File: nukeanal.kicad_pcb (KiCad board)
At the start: 2 copper layers, 85 x 56 mm, 2 parts, among them P1 CONN_13X2

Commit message: finished with schematic, footprint assignment, but no board yet
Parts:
- removed P1: CONN_13X2, pin_array_13x2
- removed sot-89: Q***, 111kicad-jake:sot-89
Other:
- board outline removed
- board text removed: "1/8" JACK OK WITH STD HEADERS !NO TH ABOVE!"
- board text removed: "DOUBLE USB CUTOUT FOR ALL BOARDS"
- board text removed: "RASPBERRY-PI ADDON BOARD VIEW FROM TOP NOTE: P1 SHOULD BE FITTED ON THE REVERSE OF THE BOARD"
- board text removed: "RCA REMOVE WITH STD HEADERS !NO TH ABOVE!"
- board text removed: "RJ45 CUTOUT FOR STD HEADERS !NO TH ABOVE!"

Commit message: merge from .zip download of jerry's latest commit
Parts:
- added C1: 100, SMD_Packages:SM0805, F.Cu at (227.0, 187.2)
- added C10: 101, SMD_Packages:SM0805, F.Cu at (200.0, 110.0)
- added C11: 104, SMD_Packages:SM0805, F.Cu at (168.8, 130.0)
- added C12: 225, SMD_Packages:SM0805, F.Cu at (165.5, 145.2)
- added C13: 225, SMD_Packages:SM0805, F.Cu at (168.8, 118.8)
- added C14: 104, SMD_Packages:SM0805, F.Cu at (165.5, 149.8)
- added C15: 225, SMD_Packages:SM0805, F.Cu at (165.5, 147.5)
- added C16: 225, SMD_Packages:SM0805, F.Cu at (232.0, 185.8)
- added C17: 225, SMD_Packages:SM0805, F.Cu at (232.0, 183.5)
- added C18: 104, SMD_Packages:SM0805, F.Cu at (177.0, 112.8)
- added C19: 225, SMD_Packages:SM0805, F.Cu at (177.0, 115.0)
- added C2: 100, SMD_Packages:SM0805, F.Cu at (197.0, 115.5)
- added C20: 104, SMD_Packages:SM0805, F.Cu at (177.0, 121.8)
- added C21: 225, SMD_Packages:SM0805, F.Cu at (177.0, 124.0)
- added C22: 104, SMD_Packages:SM0805, F.Cu at (177.0, 126.2)
- added C23: 225, SMD_Packages:SM0805, F.Cu at (177.0, 128.5)
- added C24: 104, SMD_Packages:SM0805, F.Cu at (172.5, 130.0)
- added C25: 225, SMD_Packages:SM0805, F.Cu at (172.5, 132.2)
- added C26: 104, SMD_Packages:SM0805, F.Cu at (177.0, 117.2)
- added C27: 225, SMD_Packages:SM0805, F.Cu at (177.0, 119.5)
- added C28: 104, SMD_Packages:SM0805, F.Cu at (168.8, 121.0)
- added C29: 225, SMD_Packages:SM0805, F.Cu at (168.8, 132.2)
- added C3: 225, SMD_Packages:SM0805, F.Cu at (246.8, 166.8)
- added C30: 104, SMD_Packages:SM0805, F.Cu at (173.0, 125.5)
- added C31: 225, SMD_Packages:SM0805, F.Cu at (173.0, 123.2)
- added C32: 104, SMD_Packages:SM0805, F.Cu at (177.0, 110.5)
- added C33: 225, SMD_Packages:SM0805, F.Cu at (177.0, 108.2)
- added C4: 101, SMD_Packages:SM0805, F.Cu at (252.8, 144.0)
- added C5: 104, SMD_Packages:SM0805, F.Cu at (243.2, 174.8)
- added C6: 471 poly, Capacitors_ThroughHole:Capacitor13x4RM10, F.Cu at (181.2, 135.2)
- added C7: 391, SMD_Packages:SM0805, F.Cu at (173.2, 127.8)
- added C8: 226, Capacitors:CP_5x6mm, F.Cu at (237.0, 168.0)
- added C9: 221, SMD_Packages:SM0805, F.Cu at (170.8, 172.2)
- added CU1: 104, SMD_Packages:SM0805, F.Cu at (168.8, 116.5)
- added CU2: 225, SMD_Packages:SM0805, F.Cu at (168.8, 114.2)
- added CU3: 104, SMD_Packages:SM0805, F.Cu at (228.2, 183.5)
- added CU4: 225, SMD_Packages:SM0805, F.Cu at (173.2, 119.2)
- added CU41: 104, SMD_Packages:SM0805, F.Cu at (168.8, 127.8)
- added CU5: 104, SMD_Packages:SM0805, F.Cu at (168.8, 123.2)
- added CU6: 225, SMD_Packages:SM0805, F.Cu at (168.8, 125.5)
- added CU7: 104, SMD_Packages:SM0805, F.Cu at (228.2, 181.2)
- added D1: 1N5819, Diodes_ThroughHole:Diode_DO-41_SOD81_Horizontal_RM10, F.Cu at (233.2, 161.0)
- added D10: 1N4148, Diodes_ThroughHole:Diode_DO-35_SOD27_Horizontal_RM10, F.Cu at (245.8, 156.2)
- added D11: 1N4148, Diodes_ThroughHole:Diode_DO-35_SOD27_Horizontal_RM10, F.Cu at (223.0, 117.5)
- added D12: 1N4148, Diodes_ThroughHole:Diode_DO-35_SOD27_Horizontal_RM10, F.Cu at (183.5, 172.2)
- added D13: 1N4148, Diodes_ThroughHole:Diode_DO-35_SOD27_Horizontal_RM10, F.Cu at (223.0, 124.0)
- added D14: 1N4148, Diodes_ThroughHole:Diode_DO-35_SOD27_Horizontal_RM10, F.Cu at (186.0, 167.0)
- added D2: 1N5819, Diodes_ThroughHole:Diode_DO-41_SOD81_Horizontal_RM10, F.Cu at (225.0, 176.2)
- added D3: DPAD1, 111kicad-jerry:TO-78_Housing_5Pin, F.Cu at (234.5, 150.2)
- added D5: 6.2V, Diodes_ThroughHole:Diode_DO-35_SOD27_Horizontal_RM10, F.Cu at (173.5, 165.2)
- added D6: 1N4007, Diodes_ThroughHole:Diode_DO-41_SOD81_Horizontal_RM10, F.Cu at (173.5, 148.0)
- added D7: 1N4007, Diodes_ThroughHole:Diode_DO-41_SOD81_Horizontal_RM10, F.Cu at (196.0, 175.8)
- added D8: 1N4148, Diodes_ThroughHole:Diode_DO-35_SOD27_Horizontal_RM10, F.Cu at (183.5, 177.5)
- added D9: 1N4148, Diodes_ThroughHole:Diode_DO-35_SOD27_Horizontal_RM10, F.Cu at (245.8, 151.0)
- added K1: CONN_3, Connect:SIL-3, F.Cu at (153.2, 191.4)
- added P1: BNC, 111kicad-jerry:bnc-rocket, F.Cu at (141.4, 191.2)
- added P2: CONN_1, 111kicad-jerry:testpin037, F.Cu at (197.2, 187.0)
- added P3: CONN_6, 111kicad-jerry:6x1pin037, F.Cu at (185.2, 153.5)
- added P4: CONN_2, Connect:bornier2, F.Cu at (186.2, 159.2)
- added P5: DE-9F, 111kicad-jerry:DB9FC, F.Cu at (179.3, 98.4)
- added Q1: VN3205N8-G, Discret:TO92DGS, F.Cu at (199.0, 164.5)
- added Q2: MMBT5089, Housings_SOT-23_SOT-143_TSOT-6:SOT23_Transistor_BC846_Handsoldering_RevB_14Mar2014, F.Cu at (210.5, 122.5)
- added Q3: LP0701, Discret:TO92DGS, F.Cu at (177.8, 159.2)
- added Q4: MMBT5089, Housings_SOT-23_SOT-143_TSOT-6:SOT23_Transistor_BC846_Handsoldering_RevB_14Mar2014, F.Cu at (202.2, 122.5)
- added Q5: BSS83, Transistors_SMD:sot143B, F.Cu at (209.8, 114.8)
- added Q6: BSS83, Transistors_SMD:sot143B, F.Cu at (213.2, 114.8)
- added R1: 30K, Resistors_SMD:Resistor_SMD0805_HandSoldering, F.Cu at (157.6, 188.8)
- added R10: 1K, Resistors_SMD:Resistor_SMD0805_HandSoldering, F.Cu at (205.8, 115.5)
- added R11: 422705, Resistors_SMD:Resistor_SMD0805_HandSoldering, F.Cu at (166.5, 139.5)
- added R12: 100K, Resistors_SMD:Resistor_SMD0805_HandSoldering, F.Cu at (172.0, 137.5)
- added R13: 200, Resistors_SMD:Resistor_SMD0805_HandSoldering, F.Cu at (254.2, 149.2)
- added R14: 1K, Resistors_SMD:Resistor_SMD0805_HandSoldering, F.Cu at (231.5, 118.0)
- added R15: SEL O.S., Resistors_ThroughHole:Resistor_Horizontal_RM10mm, F.Cu at (225.0, 169.2)
- added R16: 1k, Resistors_SMD:Resistor_SMD0805_HandSoldering, F.Cu at (238.5, 174.8)
- added R17: 1K, Resistors_SMD:Resistor_SMD0805_HandSoldering, F.Cu at (254.2, 154.8)
- added R18: SEL FOR LOWBATT SHUTOFF, Resistors_ThroughHole:Resistor_Horizontal_RM10mm, F.Cu at (166.8, 158.5)
- added R19: 1K, Resistors_SMD:Resistor_SMD0805_HandSoldering, F.Cu at (231.5, 124.0)
- added R2: 3K, Resistors_SMD:Resistor_SMD0805_HandSoldering, F.Cu at (157.6, 193.9)
- added R20: 47, Resistors_SMD:Resistor_SMD0805_HandSoldering, F.Cu at (231.5, 133.5)
- added R21: 47, Resistors_SMD:Resistor_SMD0805_HandSoldering, F.Cu at (193.8, 123.0)
- added R22: 10k, Resistors_SMD:Resistor_SMD0805_HandSoldering, F.Cu at (186.0, 128.2)
- added R23: 47, Resistors_SMD:Resistor_SMD0805_HandSoldering, F.Cu at (181.2, 128.2)
- added R24: 10k, Resistors_SMD:Resistor_SMD0805_HandSoldering, F.Cu at (170.2, 177.5)
- added R25: 3K, Resistors_SMD:Resistor_SMD0805_HandSoldering, F.Cu at (188.2, 119.0)
- added R26: 200, Resistors_SMD:Resistor_SMD0805_HandSoldering, F.Cu at (213.8, 111.2)
- added R27: 200, Resistors_SMD:Resistor_SMD0805_HandSoldering, F.Cu at (233.5, 176.0)
- added R28: 200, Resistors_SMD:Resistor_SMD0805_HandSoldering, F.Cu at (247.0, 161.8)
- added R29: 1M, Resistors_SMD:Resistor_SMD0805_HandSoldering, F.Cu at (209.0, 110.0)
- added R3: 27K, Resistors_SMD:Resistor_SMD0805_HandSoldering, F.Cu at (242.0, 167.2)
- added R30: 1k, Resistors_SMD:Resistor_SMD0805_HandSoldering, F.Cu at (204.2, 110.0)
- added R31: 1M, Resistors_SMD:Resistor_SMD0805_HandSoldering, F.Cu at (209.8, 104.5)
- added R32: 100, Resistors_SMD:Resistor_SMD0805_HandSoldering, F.Cu at (236.2, 133.5)
- added R33: 100, Resistors_SMD:Resistor_SMD0805_HandSoldering, F.Cu at (242.0, 161.8)
- added R34: 10k, Resistors_SMD:Resistor_SMD0805_HandSoldering, F.Cu at (198.5, 181.2)
- added R35: 100, Resistors_SMD:Resistor_SMD0805_HandSoldering, F.Cu at (175.0, 172.0)
- added R36: 10K, Resistors_SMD:Resistor_SMD0805_HandSoldering, F.Cu at (175.0, 177.5)
- added R37: 100, Resistors_SMD:Resistor_SMD0805_HandSoldering, F.Cu at (185.0, 183.0)
- added R4: 27K, Resistors_SMD:Resistor_SMD0805_HandSoldering, F.Cu at (163.2, 189.0)
- added R5: 240, Resistors_SMD:Resistor_SMD0805_HandSoldering, F.Cu at (168.7, 189.0)
- added R6: 100, Resistors_SMD:Resistor_SMD0805_HandSoldering, F.Cu at (205.0, 104.5)
- added R7: 22M, Resistors_SMD:Resistor_SMD0805_HandSoldering, F.Cu at (165.0, 165.2)
- added R8: 1K, Resistors_SMD:Resistor_SMD0805_HandSoldering, F.Cu at (201.0, 115.5)
- added R9: 10-30 for -.5V, Resistors_ThroughHole:Resistor_Horizontal_RM10mm, F.Cu at (235.5, 140.2)
- added SW1: ONOFF, Pin_Headers:Pin_Header_Straight_1x02, F.Cu at (192.8, 181.5)
- added U1: OPA2365, Power_Integrations:SO-8, F.Cu at (166.4, 194.5)
- added U10: 74HC14, SMD_Packages:SO14N, F.Cu at (209.8, 156.2)
- added U11: 74HC74j, SMD_Packages:SO14N, F.Cu at (198.8, 156.2)
- added U2: MIC5209-3.3, 111kicad-jerry:SOT-223-3, F.Cu at (184.2, 145.8)
- added U3: MIC5219YM5TR, SMD_Packages:SOT23-5, F.Cu at (172.5, 140.8)
- added U4: REF5045, Power_Integrations:SO-8, F.Cu at (221.8, 163.8)
- added U5: MIC5209-2.5, 111kicad-jerry:SOT-223-3, F.Cu at (192.8, 132.8)
- added U6: OPA2365, Power_Integrations:SO-8, F.Cu at (193.0, 148.0)
- added U7: 74HC14, SMD_Packages:SO14N, F.Cu at (209.2, 164.0)
- added U8: LM311N, Power_Integrations:SO-8, F.Cu at (193.0, 140.5)
- added U9: AD7983, SMD_Packages:MSOP10-0.5, F.Cu at (225.8, 155.5)
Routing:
- net Net-(C1-Pad1): track 0.00 -> 17.4 mm
- net +5.25V: track 0.00 -> 15.8 mm
- net Net-(R2-Pad1): track 0.00 -> 14.5 mm
- net Net-(C1-Pad2): track 0.00 -> 12.5 mm
- net Net-(C2-Pad2): track 0.00 -> 10.4 mm
- net Net-(K1-Pad3): track 0.00 -> 3.11 mm
- net Net-(K1-Pad1): track 0.00 -> 3.11 mm
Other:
- board outline added: 169.9 x 108.7 mm

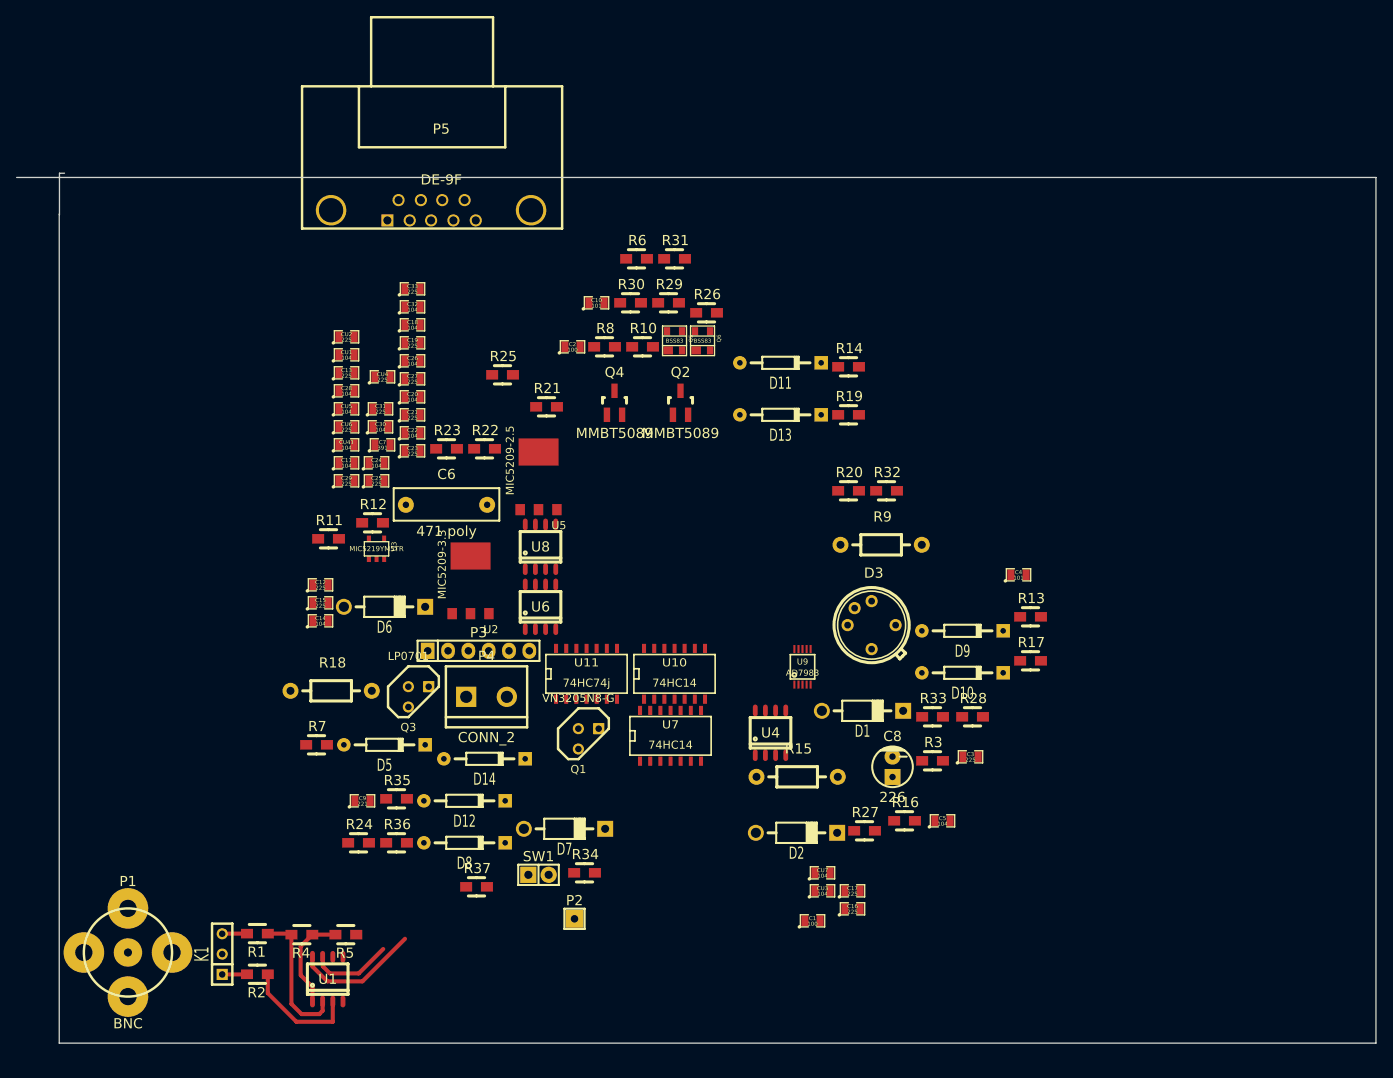
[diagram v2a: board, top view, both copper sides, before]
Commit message: used a zip to force merge to jakes latest work
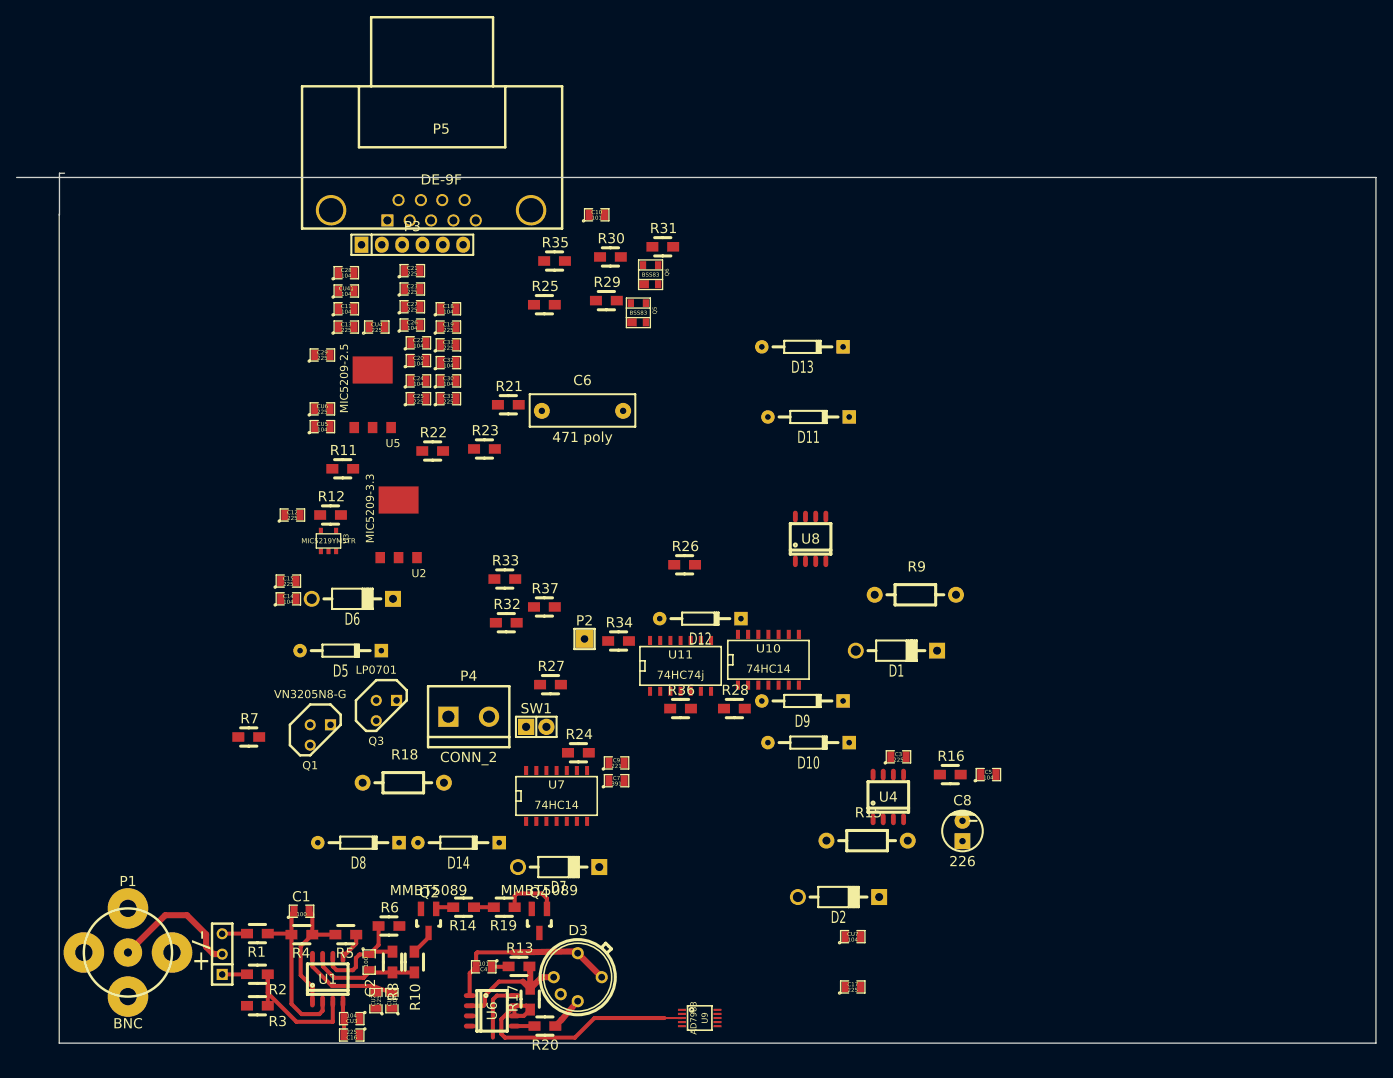
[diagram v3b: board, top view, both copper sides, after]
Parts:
- moved R3 89.8 mm to (157.6, 197.9)
- moved R6 89.0 mm to (174.1, 187.9)
- moved CU2 83.1 mm to (172.4, 197.2), turned to 90 degrees
- moved R14 82.9 mm to (183.4, 185.5), turned to 180 degrees
- moved C4 82.9 mm to (185.9, 193.0), turned to 180 degrees
- moved R10 82.0 mm to (177.2, 192.4), turned to 270 degrees
- moved R8 81.3 mm to (174.5, 192.4), turned to 90 degrees
- moved C2 81.0 mm to (171.6, 192.4), turned to 270 degrees
- moved CU1 80.9 mm to (174.4, 197.2), turned to 90 degrees
- moved R13 77.5 mm to (190.3, 192.9)
- moved R20 76.9 mm to (193.5, 200.4), turned to 180 degrees
- moved R17 75.5 mm to (191.7, 197.0), turned to 90 degrees
- moved R19 75.1 mm to (188.5, 185.5), turned to 180 degrees
- moved Q2 72.0 mm to (179.0, 187.3), turned to 180 degrees
- moved R35 70.1 mm to (194.8, 104.8)
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- renumbered K1 to +/-
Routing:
- net Net-(R17-Pad1): track 0.00 -> 33.8 mm
- net Net-(C4-Pad2): track 0.00 -> 22.7 mm
- net Net-(K1-Pad2): track 0.00 -> 16.6 mm
- net Net-(D3-Pad2): track 0.00 -> 16.2 mm
- net Net-(C2-Pad1): track 0.00 -> 14.5 mm
- net Net-(Q4-PadB): track 0.00 -> 7.13 mm
- net +5.25V: track 15.8 -> 21.1 mm
- net -0.25V: track 0.00 -> 4.25 mm
- net Net-(D3-Pad5): track 0.00 -> 4.19 mm
- net Net-(R2-Pad1): track 14.5 -> 18.4 mm
- net Net-(C2-Pad2): track 10.4 -> 14.0 mm
- net Net-(R5-Pad1): track 0.00 -> 3.45 mm
- net Net-(C1-Pad2): track 12.5 -> 15.5 mm
- net Net-(Q2-PadC): track 0.00 -> 3.08 mm
- net Net-(C1-Pad1): track 17.4 -> 20.5 mm
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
